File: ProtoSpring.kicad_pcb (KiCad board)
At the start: 2 copper layers, 100 x 50 mm, 41 parts, among them P1 CONN_3X2, P10 CONN_14, P11 CONN_14, P12 CONN_14, P13 CONN_14, P14 CONN_14, P15 CONN_14, P16 CONN_14, P17 CONN_14, P18 CONN_14, P19 CONN_14, P2 CONN_7X2, P20 CONN_14, P21 CONN_14, P22 CONN_14, P23 CONN_14, P24 CONN_14, P25 CONN_14, P26 CONN_14, P27 CONN_14, P3 CONN_4X2, P4 CONN_3X2, P5 CONN_8X2, P6 CONN_2X2, P7 CONN_4X2, P8 CONN_14, P9 CONN_14

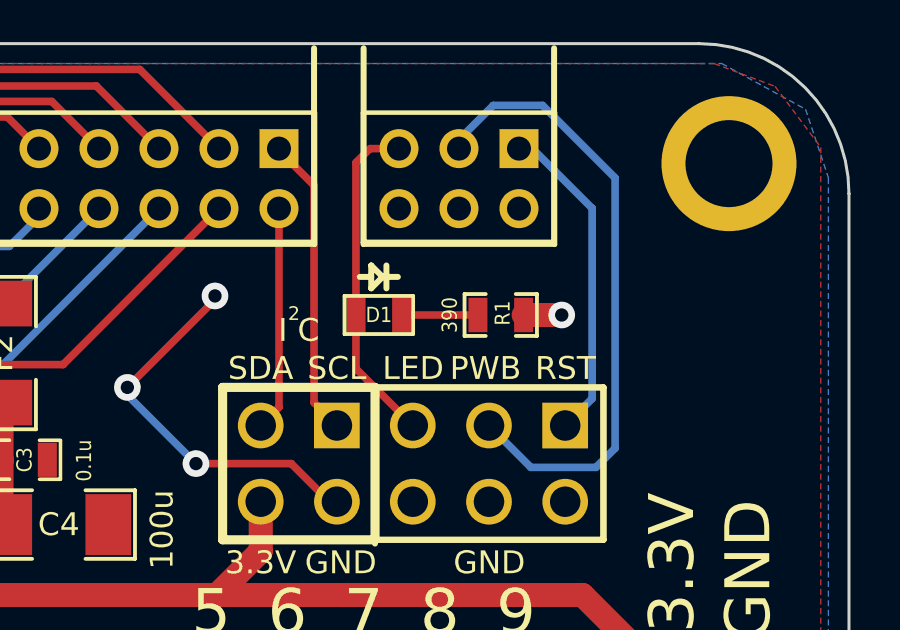
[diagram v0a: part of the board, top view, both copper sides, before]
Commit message: update schematics and pcb with some lessons learned
Brief changelog:

* add manufacturers and part numbers for recommended parts
* change current limiting resistor for LED to fit its current requirements
* update PCB with new resistor value
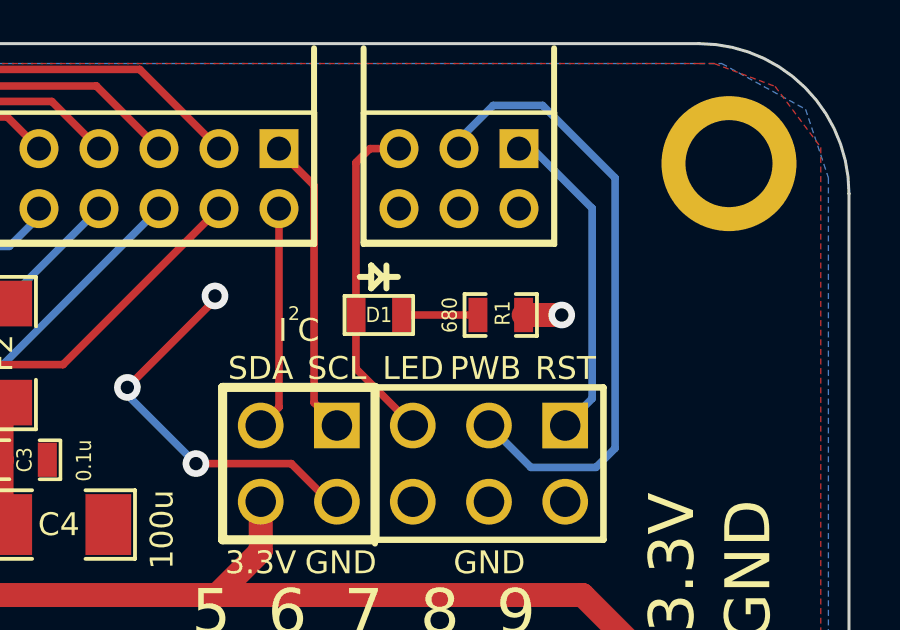
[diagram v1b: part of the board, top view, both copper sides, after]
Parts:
- R1: value 390 -> 680
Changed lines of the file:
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@@
       (effects (font (size 0.50038 0.4572) (thickness 0.1143)))
     )
-    (fp_text value 390 (at -1.69926 0 90) (layer F.SilkS)
+    (fp_text value 680 (at -1.69926 0 90) (layer F.SilkS)
       (effects (font (size 0.508 0.4572) (thickness 0.1143)))
     )

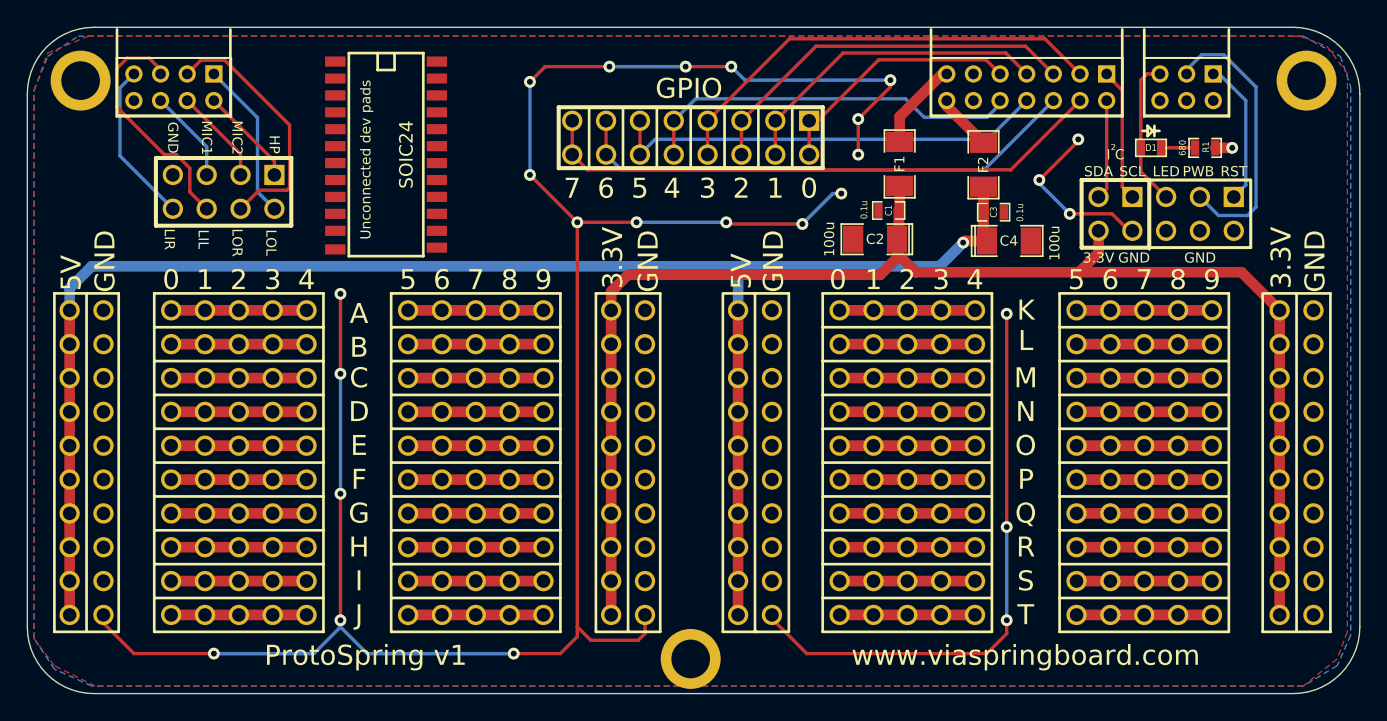
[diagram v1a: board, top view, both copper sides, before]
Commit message: adjusting the paths for the Audio headers
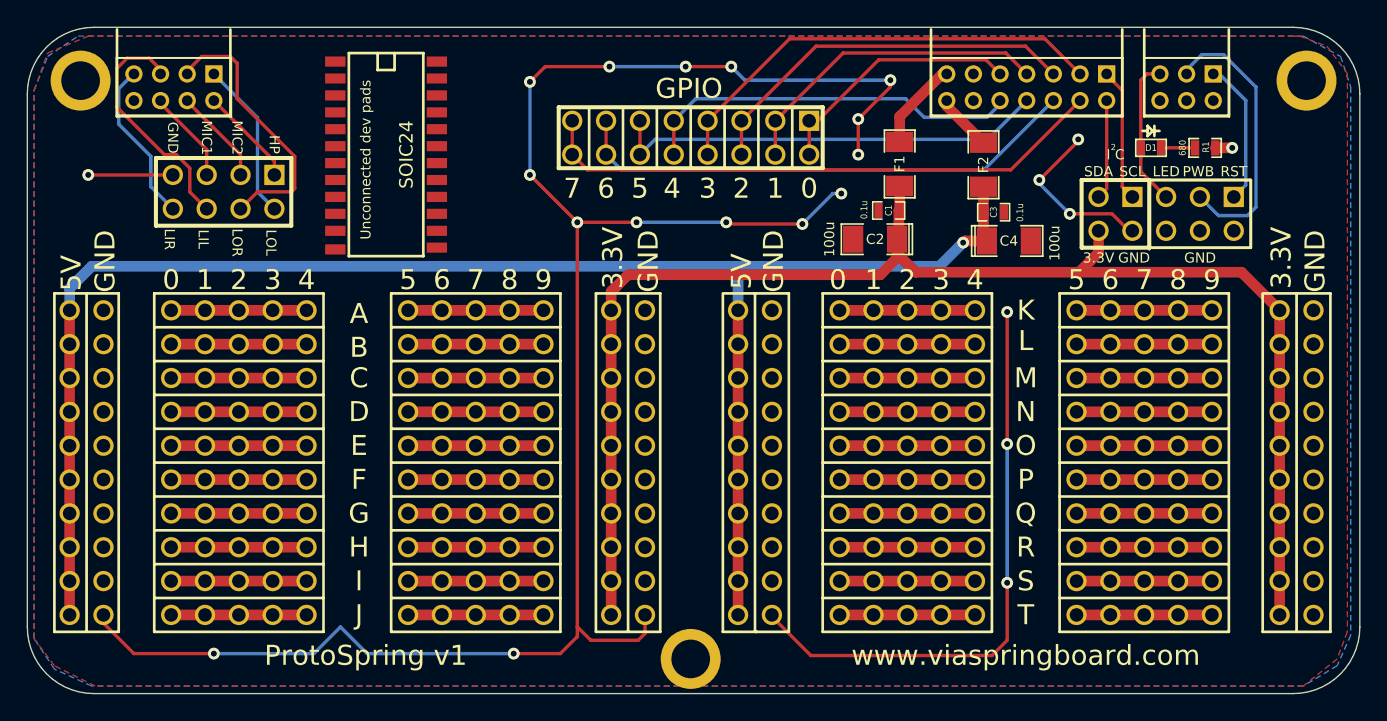
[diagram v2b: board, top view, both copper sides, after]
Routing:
- net GND: track 227.8 -> 209.7 mm, vias 26 -> 23
- net /LINEOUT_R: track 19.2 -> 20.5 mm
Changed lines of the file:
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@@
     (thickness 1.6)
     (drawings 190)
-    (tracks 403)
+    (tracks 404)
     (zones 0)
     (modules 41)
@@
   (segment (start 208 108.5) (end 208 108.559) (width 0.254) (layer F.Cu) (net 13))
   (segment (start 137 108.5) (end 137 108.171) (width 0.254) (layer F.Cu) (net 14))
+  (segment (start 137 108.171) (end 136.144 107.315) (width 0.254) (layer F.Cu) (net 14))
+  (segment (start 136.144 107.315) (end 134.493 107.315) (width 0.254) (layer F.Cu) (net 14))
+  (segment (start 134.493 107.315) (end 133.731 108.077) (width 0.254) (layer F.Cu) (net 14))
+  (segment (start 133.731 108.077) (end 133.731 110.998) (width 0.254) (layer F.Cu) (net 14))
+  (segment (start 133.731 110.998) (end 137.287 114.554) (width 0.254) (layer F.Cu) (net 14))
+  (segment (start 137.287 114.554) (end 138.176 114.554) (width 0.254) (layer F.Cu) (net 14))
+  (segment (start 138.176 114.554) (end 139.192 115.57) (width 0.254) (layer F.Cu) (net 14))
+  (segment (start 139.192 115.57) (end 139.192 117.348) (width 0.254) (layer F.Cu) (net 14))
   (segment (start 139.192 117.348) (end 140.462 118.618) (width 0.254) (layer F.Cu) (net 14))
-  (segment (start 139.192 115.57) (end 139.192 117.348) (width 0.254) (layer F.Cu) (net 14))
-  (segment (start 138.176 114.554) (end 139.192 115.57) (width 0.254) (layer F.Cu) (net 14))
-  (segment (start 137.287 114.554) (end 138.176 114.554) (width 0.254) (layer F.Cu) (net 14))
-  (segment (start 133.731 110.998) (end 137.287 114.554) (width 0.254) (layer F.Cu) (net 14))
-  (segment (start 133.731 108.077) (end 133.731 110.998) (width 0.254) (layer F.Cu) (net 14))
-  (segment (start 134.493 107.315) (end 133.731 108.077) (width 0.254) (layer F.Cu) (net 14))
-  (segment (start 136.144 107.315) (end 134.493 107.315) (width 0.254) (layer F.Cu) (net 14))
-  (segment (start 137 108.171) (end 136.144 107.315) (width 0.254) (layer F.Cu) (net 14))
-  (segment (start 133.9546 114.6506) (end 137.922 118.618) (width 0.254) (layer B.Cu) (net 15))
-  (segment (start 133.9546 109.5454) (end 133.9546 114.6506) (width 0.254) (layer B.Cu) (net 15))
-  (segment (start 135 108.5) (end 133.9546 109.5454) (width 0.254) (layer B.Cu) (net 15))
+  (segment (start 135 108.5) (end 134.959 108.5) (width 0.254) (layer B.Cu) (net 15))
+  (segment (start 136.271 116.967) (end 137.922 118.618) (width 0.254) (layer B.Cu) (net 15))
+  (segment (start 136.271 114.681) (end 136.271 116.967) (width 0.254) (layer B.Cu) (net 15))
+  (segment (start 133.858 112.268) (end 136.271 114.681) (width 0.254) (layer B.Cu) (net 15))
+  (segment (start 133.858 109.601) (end 133.858 112.268) (width 0.254) (layer B.Cu) (net 15))
+  (segment (start 134.959 108.5) (end 133.858 109.601) (width 0.254) (layer B.Cu) (net 15))
   (segment (start 144.272 117.348) (end 145.542 118.618) (width 0.254) (layer B.Cu) (net 16))
   (segment (start 144.272 111.772) (end 144.272 117.348) (width 0.254) (layer B.Cu) (net 16))
   (segment (start 141 108.5) (end 144.272 111.772) (width 0.254) (layer B.Cu) (net 16))
-  (segment (start 144.3986 117.2214) (end 143.002 118.618) (width 0.254) (layer F.Cu) (net 17))
-  (segment (start 146.4892 117.2214) (end 144.3986 117.2214) (width 0.254) (layer F.Cu) (net 17))
-  (segment (start 146.6853 117.0253) (end 146.4892 117.2214) (width 0.254) (layer F.Cu) (net 17))
-  (segment (start 146.6853 112.3347) (end 146.6853 117.0253) (width 0.254) (layer F.Cu) (net 17))
-  (segment (start 141.8192 107.4686) (end 146.6853 112.3347) (width 0.254) (layer F.Cu) (net 17))
-  (segment (start 140.0314 107.4686) (end 141.8192 107.4686) (width 0.254) (layer F.Cu) (net 17))
-  (segment (start 139 108.5) (end 140.0314 107.4686) (width 0.254) (layer F.Cu) (net 17))
-  (segment (start 140.462 113.962) (end 140.462 116.078) (width 0.254) (layer B.Cu) (net 18))
-  (segment (start 137 110.5) (end 140.462 113.962) (width 0.254) (layer B.Cu) (net 18))
-  (segment (start 143.002 114.502) (end 143.002 116.078) (width 0.254) (layer F.Cu) (net 19))
-  (segment (start 139 110.5) (end 143.002 114.502) (width 0.254) (layer F.Cu) (net 19))
+  (segment (start 144.272 117.348) (end 143.002 118.618) (width 0.254) (layer F.Cu) (net 17))
+  (segment (start 146.812 117.348) (end 144.272 117.348) (width 0.254) (layer F.Cu) (net 17))
+  (segment (start 147.066 117.094) (end 146.812 117.348) (width 0.254) (layer F.Cu) (net 17))
+  (segment (start 147.066 114.681) (end 147.066 117.094) (width 0.254) (layer F.Cu) (net 17))
+  (segment (start 142.748 110.363) (end 147.066 114.681) (width 0.254) (layer F.Cu) (net 17))
+  (segment (start 142.748 107.696) (end 142.748 110.363) (width 0.254) (layer F.Cu) (net 17))
+  (segment (start 142.24 107.188) (end 142.748 107.696) (width 0.254) (layer F.Cu) (net 17))
+  (segment (start 140.081 107.188) (end 142.24 107.188) (width 0.254) (layer F.Cu) (net 17))
+  (segment (start 139 108.269) (end 140.081 107.188) (width 0.254) (layer F.Cu) (net 17))
+  (segment (start 139 108.5) (end 139 108.269) (width 0.254) (layer F.Cu) (net 17))
+  (segment (start 137 110.5) (end 137 110.711) (width 0.254) (layer F.Cu) (net 18))
+  (segment (start 140.462 114.173) (end 140.462 116.078) (width 0.254) (layer F.Cu) (net 18))
+  (segment (start 137 110.711) (end 140.462 114.173) (width 0.254) (layer F.Cu) (net 18))
+  (segment (start 139 110.5) (end 139 110.552) (width 0.254) (layer F.Cu) (net 19))
+  (segment (start 143.002 114.554) (end 143.002 116.078) (width 0.254) (layer F.Cu) (net 19))
+  (segment (start 139 110.552) (end 143.002 114.554) (width 0.254) (layer F.Cu) (net 19))
   (segment (start 214 108.5) (end 214 108.199) (width 0.254) (layer B.Cu) (net 20))
   (segment (start 216.396 119.126) (end 215 117.73) (width 0.254) (layer B.Cu) (net 20))
@@
   (segment (start 218.44 110.49) (end 218.44 116.83) (width 0.254) (layer B.Cu) (net 22))
   (segment (start 216.45 108.5) (end 218.44 110.49) (width 0.254) (layer B.Cu) (net 22))
+  (segment (start 137.922 116.078) (end 131.572 116.078) (width 0.254) (layer F.Cu) (net 23))
+  (via (at 131.572 116.078) (size 0.889) (layers F.Cu B.Cu) (net 23))
+  (segment (start 182.88 149.098) (end 182.88 149.225) (width 0.254) (layer F.Cu) (net 23))
+  (via (at 200.533 126.365) (size 0.889) (layers F.Cu B.Cu) (net 23))
+  (segment (start 200.533 136.271) (end 200.533 126.365) (width 0.254) (layer F.Cu) (net 23))
+  (via (at 200.533 136.271) (size 0.889) (layers F.Cu B.Cu) (net 23))
+  (segment (start 200.533 146.685) (end 200.533 136.271) (width 0.254) (layer B.Cu) (net 23))
+  (via (at 200.533 146.685) (size 0.889) (layers F.Cu B.Cu) (net 23))
+  (segment (start 200.533 151.003) (end 200.533 146.685) (width 0.254) (layer F.Cu) (net 23))
+  (segment (start 199.39 152.146) (end 200.533 151.003) (width 0.254) (layer F.Cu) (net 23))
+  (segment (start 185.801 152.146) (end 199.39 152.146) (width 0.254) (layer F.Cu) (net 23))
+  (segment (start 182.88 149.225) (end 185.801 152.146) (width 0.254) (layer F.Cu) (net 23))
   (segment (start 168.275 149.987) (end 168.275 150.725) (width 0.254) (layer F.Cu) (net 23))
   (segment (start 152.5 152) (end 150.5 150) (width 0.254) (layer B.Cu) (net 23))
@@
   (segment (start 167 152) (end 163.5 152) (width 0.254) (layer F.Cu) (net 23))
   (segment (start 168.275 150.725) (end 167 152) (width 0.254) (layer F.Cu) (net 23))
-  (segment (start 182.88 149.098) (end 182.88 149.38) (width 0.254) (layer F.Cu) (net 23))
-  (via (at 200.5 126.5) (size 0.889) (layers F.Cu B.Cu) (net 23))
-  (segment (start 200.5 132.5) (end 200.5 126.5) (width 0.254) (layer F.Cu) (net 23))
-  (segment (start 200.5 142.5) (end 200.5 132.5) (width 0.254) (layer F.Cu) (net 23))
-  (via (at 200.5 142.5) (size 0.889) (layers F.Cu B.Cu) (net 23))
-  (segment (start 200.5 149.5) (end 200.5 142.5) (width 0.254) (layer B.Cu) (net 23))
-  (via (at 200.5 149.5) (size 0.889) (layers F.Cu B.Cu) (net 23))
-  (segment (start 200.5 150.5) (end 200.5 149.5) (width 0.254) (layer F.Cu) (net 23))
-  (segment (start 199 152) (end 200.5 150.5) (width 0.254) (layer F.Cu) (net 23))
-  (segment (start 185.5 152) (end 199 152) (width 0.254) (layer F.Cu) (net 23))
-  (segment (start 182.88 149.38) (end 185.5 152) (width 0.254) (layer F.Cu) (net 23))
   (segment (start 132.715 149.098) (end 132.715 149.715) (width 0.254) (layer F.Cu) (net 23))
   (segment (start 132.715 149.715) (end 135 152) (width 0.254) (layer F.Cu) (net 23))
@@
   (segment (start 141 152) (end 148.5 152) (width 0.254) (layer B.Cu) (net 23))
   (segment (start 148.5 152) (end 150.5 150) (width 0.254) (layer B.Cu) (net 23))
-  (via (at 150.5 125) (size 0.889) (layers F.Cu B.Cu) (net 23))
-  (segment (start 150.5 150) (end 150.5 149.5) (width 0.254) (layer B.Cu) (net 23))
-  (via (at 150.5 149.5) (size 0.889) (layers F.Cu B.Cu) (net 23))
-  (segment (start 150.5 149.5) (end 150.5 140) (width 0.254) (layer F.Cu) (net 23))
-  (via (at 150.5 140) (size 0.889) (layers F.Cu B.Cu) (net 23))
-  (segment (start 150.5 140) (end 150.5 131) (width 0.254) (layer B.Cu) (net 23))
-  (via (at 150.5 131) (size 0.889) (layers F.Cu B.Cu) (net 23))
-  (segment (start 150.5 131) (end 150.5 125) (width 0.254) (layer F.Cu) (net 23))
   (via (at 168.275 119.634) (size 0.889) (layers F.Cu B.Cu) (net 23))
   (segment (start 168.275 119.634) (end 168.275 119.761) (width 0.254) (layer B.Cu) (net 23))
